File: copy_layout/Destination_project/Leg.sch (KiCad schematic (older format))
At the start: 10 parts, among them Q1 CSD19531KCS, Q2 CSD19531KCS, U2 IR2181, U3 LTS_15

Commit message: Delna verzija
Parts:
- removed C1, C2, C3: 100n, Passives:C1206M, symbol Passives:C1206
- removed D1: LL4148, Discretes:D_MiniMELF, symbol Discretes:LL4148
- removed Q1, Q2: CSD19531KCS, Discretes:TO-220, symbol Discretes:CSD19531KCS
- removed R1, R2: 22R, Passives:R1206M, symbol Passives:R1206
- removed U2: IR2181, Package_SO:SO8, symbol ICs:IR2181
- removed U3: LTS_15, Sensor_Current:LTS_15, symbol Sensor_Current:LTS_15
- added J1, J2: Pusa_4mm, Connector:Pusa_4mm, symbol Connector:Pusa_4mm
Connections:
- new net Power-/OUT: J2.1 (Pin_1)
- new net Sensor/OUT: J1.1 (Pin_1)

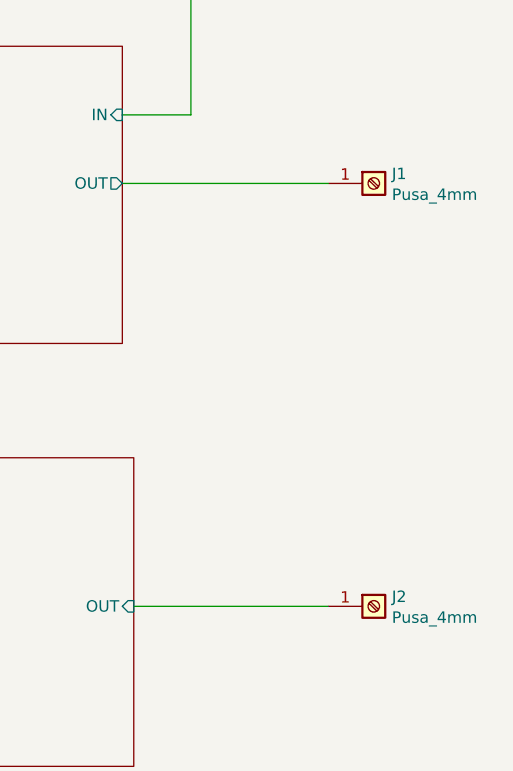
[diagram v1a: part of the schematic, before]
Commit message: Modified test project. Successfule began importing layout
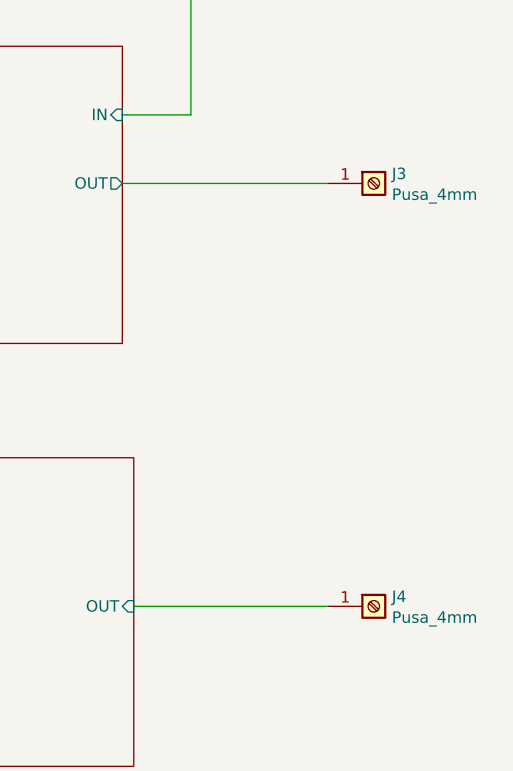
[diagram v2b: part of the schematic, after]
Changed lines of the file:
@@
 $Descr A4 11693 8268
 encoding utf-8
-Sheet 3 6
+Sheet 7 10
 Title ""
 Date ""
@@
 AR Path="/5B76D031/5B772913" Ref="J?"  Part="1"
 AR Path="/5CADA6B4/5B772913" Ref="J1"  Part="1"
-F 0 "J1" H 7129 4042 50  0000 L CNN
+AR Path="/5CAF0FB9/5B772913" Ref="J3"  Part="1"
+F 0 "J3" H 7129 4042 50  0000 L CNN
 F 1 "Pusa_4mm" H 7129 3951 50  0000 L CNN
 F 2 "Connector:Pusa_4mm" H 7125 3950 50  0001 L CNN
@@
 AR Path="/5B76D031/5B77299E" Ref="J?"  Part="1"
 AR Path="/5CADA6B4/5B77299E" Ref="J2"  Part="1"
-F 0 "J2" H 7129 5892 50  0000 L CNN
+AR Path="/5CAF0FB9/5B77299E" Ref="J4"  Part="1"
+F 0 "J4" H 7129 5892 50  0000 L CNN
 F 1 "Pusa_4mm" H 7129 5801 50  0000 L CNN
 F 2 "Connector:Pusa_4mm" H 7125 5800 50  0001 L CNN
